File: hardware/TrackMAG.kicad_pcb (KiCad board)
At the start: 4 copper layers, 36 x 36 mm, 54 parts, among them J1 USB_C_Socket_USB2.0, J2 Conn_Debug, SW1 SW_RESET, SW2 SW_BOOT, U1 LSM6DS3TR-C, U2 USBLC6-2P6, U3 STM32F103C8T6, U4 LIS2MDL, U5 AMS1117-3.3, Y1 16MHz

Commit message: Cleanup
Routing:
- net GND: vias 41 -> 44
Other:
- board text added: "TrackMAG v1"
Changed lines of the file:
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@@
     (property "Sheetfile" "TrackMAG.kicad_sch")
     (property "Sheetname" "")
+    (property "exclude_from_bom" "")
     (property "ki_description" "Mounting Hole without connection")
     (property "ki_keywords" "mounting hole")
-    (attr exclude_from_pos_files)
+    (attr exclude_from_pos_files exclude_from_bom)
     (fp_text reference "H2" (at 0 -3.2) (layer "F.SilkS") hide
         (effects (font (size 1 1) (thickness 0.15)))
@@
     (fp_line (start 1 0.625) (end -1 0.625)
       (stroke (width 0.1) (type solid)) (layer "F.Fab"))
-    (pad "1" smd roundrect (at -0.9125 0 90) (size 1.025 1.4) (layers "F.Cu" "F.Paste" "F.Mask") (roundrect_rratio 0.243902)
+    (pad "1" smd roundrect (at -0.9125 0 90) (size 1.025 1.4) (layers "F.Cu" "F.Paste" "F.Mask") (roundrect_rratio 0.243902439)
       (net 6 "VBUS") (pintype "passive"))
-    (pad "2" smd roundrect (at 0.9125 0 90) (size 1.025 1.4) (layers "F.Cu" "F.Paste" "F.Mask") (roundrect_rratio 0.243902)
+    (pad "2" smd roundrect (at 0.9125 0 90) (size 1.025 1.4) (layers "F.Cu" "F.Paste" "F.Mask") (roundrect_rratio 0.243902439)
       (net 57 "+5V") (pintype "passive"))
     (model "${KICAD6_3DMODEL_DIR}/Resistor_SMD.3dshapes/R_0805_2012Metric.wrl"
@@
     (fp_line (start 1.6 0.8) (end 1.6 -0.8)
       (stroke (width 0.1) (type solid)) (layer "F.Fab"))
-    (pad "1" smd roundrect (at -1.35 0) (size 1.4 1.35) (layers "F.Cu" "F.Paste" "F.Mask") (roundrect_rratio 0.185185)
+    (pad "1" smd roundrect (at -1.35 0) (size 1.4 1.35) (layers "F.Cu" "F.Paste" "F.Mask") (roundrect_rratio 0.1851851852)
       (net 6 "VBUS") (pintype "passive"))
-    (pad "2" smd roundrect (at 1.35 0) (size 1.4 1.35) (layers "F.Cu" "F.Paste" "F.Mask") (roundrect_rratio 0.185185)
+    (pad "2" smd roundrect (at 1.35 0) (size 1.4 1.35) (layers "F.Cu" "F.Paste" "F.Mask") (roundrect_rratio 0.1851851852)
       (net 2 "GND") (pintype "passive"))
     (model "${KICAD6_3DMODEL_DIR}/Capacitor_Tantalum_SMD.3dshapes/CP_EIA-3216-18_Kemet-A.wrl"
@@
     (descr "LED SMD 0603 (1608 Metric), square (rectangular) end terminal, IPC_7351 nominal, (Body size source: http://www.tortai-tech.com/upload/download/2011102023233369053.pdf), generated with kicad-footprint-generator")
     (tags "LED")
+    (property "JLCPCB Part #" "C2286")
     (property "Sheetfile" "TrackMAG.kicad_sch")
     (property "Sheetname" "")
@@
     (property "Sheetfile" "TrackMAG.kicad_sch")
     (property "Sheetname" "")
+    (property "exclude_from_bom" "")
     (property "ki_description" "Mounting Hole without connection")
     (property "ki_keywords" "mounting hole")
-    (attr exclude_from_pos_files)
+    (attr exclude_from_pos_files exclude_from_bom)
     (fp_text reference "H1" (at 0 -3.2) (layer "F.SilkS") hide
         (effects (font (size 1 1) (thickness 0.15)))
@@
     (fp_line (start 1.6 0.8) (end 1.6 -0.8)
       (stroke (width 0.1) (type solid)) (layer "F.Fab"))
-    (pad "1" smd roundrect (at -1.35 0) (size 1.4 1.35) (layers "F.Cu" "F.Paste" "F.Mask") (roundrect_rratio 0.185185)
+    (pad "1" smd roundrect (at -1.35 0) (size 1.4 1.35) (layers "F.Cu" "F.Paste" "F.Mask") (roundrect_rratio 0.1851851852)
       (net 1 "+3.3V") (pintype "passive"))
-    (pad "2" smd roundrect (at 1.35 0) (size 1.4 1.35) (layers "F.Cu" "F.Paste" "F.Mask") (roundrect_rratio 0.185185)
+    (pad "2" smd roundrect (at 1.35 0) (size 1.4 1.35) (layers "F.Cu" "F.Paste" "F.Mask") (roundrect_rratio 0.1851851852)
       (net 2 "GND") (pintype "passive"))
     (model "${KICAD6_3DMODEL_DIR}/Capacitor_Tantalum_SMD.3dshapes/CP_EIA-3216-18_Kemet-A.wrl"
@@
     (property "Sheetfile" "TrackMAG.kicad_sch")
     (property "Sheetname" "")
+    (property "exclude_from_bom" "")
     (property "ki_description" "Mounting Hole without connection")
     (property "ki_keywords" "mounting hole")
-    (attr exclude_from_pos_files)
+    (attr exclude_from_pos_files exclude_from_bom)
     (fp_text reference "H3" (at 0 -3.2) (layer "F.SilkS") hide
         (effects (font (size 1 1) (thickness 0.15)))
@@
   (gr_line (start 40.8 68) (end 70.8 68)
     (stroke (width 0.1) (type default)) (layer "Edge.Cuts"))
+  (gr_text "TrackMAG v1" (at 38.25 37.25 -90) (layer "F.SilkS" knockout)
+    (effects (font (size 1 1) (thickness 0.2) bold) (justify left bottom))
+  )
   (segment (start 51.4 39.95) (end 51.4 33.975) (width 0.3) (layer "F.Cu") (net 1))
   (segment (start 45.8 42.575) (end 45.8 42.7) (width 0.3) (layer "F.Cu") (net 1))
@@
   (segment (start 52.15 33.225) (end 46.875 33.225) (width 0.3) (layer "F.Cu") (net 1))
   (segment (start 44.75 44.8045) (end 44.75 46.075) (width 0.3) (layer "F.Cu") (net 1))
-  (segment (start 43.86 34.302943) (end 44.937943 33.225) (width 0.3) (layer "F.Cu") (net 1))
   (segment (start 65.9875 59.0625) (end 66.3875 59.4625) (width 0.2) (layer "F.Cu") (net 1))
   (segment (start 56.8875 54.6875) (end 56.8875 53.717165) (width 0.3) (layer "F.Cu") (net 1))
@@
   (segment (start 49.6 45) (end 49.6 44.7) (width 0.3) (layer "F.Cu") (net 1))
   (segment (start 52.775 41.425) (end 52.825 41.375) (width 0.3) (layer "F.Cu") (net 1))
+  (segment (start 43.8305 34.332443) (end 44.937943 33.225) (width 0.3) (layer "F.Cu") (net 1))
   (segment (start 53.3875 56.3105) (end 53.477 56.4) (width 0.3) (layer "F.Cu") (net 1))
   (segment (start 62.45 56.635) (end 66.385 56.635) (width 0.3) (layer "F.Cu") (net 1))
@@
   (segment (start 67.0625 58.3375) (end 66.1425 58.3375) (width 0.3) (layer "F.Cu") (net 1))
   (segment (start 67.3875 60.9875) (end 67.3875 61.5375) (width 0.25) (layer "F.Cu") (net 1))
-  (segment (start 43.86 40.635) (end 43.86 34.302943) (width 0.3) (layer "F.Cu") (net 1))
   (segment (start 45 65.125) (end 43.05 63.175) (width 0.3) (layer "F.Cu") (net 1))
   (segment (start 52.298 56.4) (end 51.375 57.323) (width 0.3) (layer "F.Cu") (net 1))
@@
   (segment (start 59.875 47.775) (end 60.075 47.575) (width 0.3) (layer "F.Cu") (net 1))
   (segment (start 49.55 57.99) (end 50.135 58.575) (width 0.3) (layer "F.Cu") (net 1))
+  (segment (start 45.8 42.625) (end 43.8305 40.6555) (width 0.3) (layer "F.Cu") (net 1))
   (segment (start 39.475 54.025) (end 38.725 53.275) (width 0.3) (layer "F.Cu") (net 1))
   (segment (start 46.425 47.75) (end 48.17 47.75) (width 0.3) (layer "F.Cu") (net 1))
@@
   (segment (start 48.17 47.75) (end 48.175 47.755) (width 0.3) (layer "F.Cu") (net 1))
   (segment (start 60.075 44.6) (end 60.075 47.575) (width 0.3) (layer "F.Cu") (net 1))
+  (segment (start 43.8305 40.6555) (end 43.8305 34.332443) (width 0.3) (layer "F.Cu") (net 1))
   (segment (start 67.3875 61.5375) (end 67.125 61.8) (width 0.25) (layer "F.Cu") (net 1))
   (segment (start 67.8875 63.5325) (end 68.2925 63.5325) (width 0.3) (layer "F.Cu") (net 1))
@@
   (segment (start 68.5 63.325) (end 68.5 61.8) (width 0.3) (layer "F.Cu") (net 1))
   (segment (start 45.2 65.125) (end 51.2 65.125) (width 0.3) (layer "F.Cu") (net 1))
-  (segment (start 43.86 40.635) (end 45.8 42.575) (width 0.3) (layer "F.Cu") (net 1))
   (segment (start 66.3875 56.6375) (end 66.3875 58.0925) (width 0.3) (layer "F.Cu") (net 1))
   (segment (start 63.88 60.725) (end 65.125 60.725) (width 0.25) (layer "F.Cu") (net 1))
@@
   (segment (start 63.2175 57.9025) (end 63.0775 57.7625) (width 0.3) (layer "F.Cu") (net 2))
   (via (at 54.5 56.4) (size 0.8) (drill 0.4) (layers "F.Cu" "B.Cu") (free) (net 2))
+  (via (at 49.55 54.2) (size 0.8) (drill 0.4) (layers "F.Cu" "B.Cu") (free) (net 2))
   (via (at 49.135497 58.575) (size 0.8) (drill 0.4) (layers "F.Cu" "B.Cu") (free) (net 2))
   (via (at 65.4125 61.7875) (size 0.8) (drill 0.4) (layers "F.Cu" "B.Cu") (net 2))
@@
   (via (at 55.638553 53.373315) (size 0.8) (drill 0.4) (layers "F.Cu" "B.Cu") (net 2))
   (via (at 44.75 42.625) (size 0.8) (drill 0.4) (layers "F.Cu" "B.Cu") (free) (net 2))
+  (via (at 58.475 55.8) (size 0.8) (drill 0.4) (layers "F.Cu" "B.Cu") (free) (net 2))
   (via (at 63.575 54.15) (size 0.8) (drill 0.4) (layers "F.Cu" "B.Cu") (net 2))
   (via (at 43.875 45.4) (size 0.8) (drill 0.4) (layers "F.Cu" "B.Cu") (free) (net 2))
@@
   (via (at 57.375 42.5) (size 0.8) (drill 0.4) (layers "F.Cu" "B.Cu") (free) (net 2))
   (via (at 71.525 50.025) (size 0.8) (drill 0.4) (layers "F.Cu" "B.Cu") (net 2))
+  (via (at 44.4705 39.7) (size 0.8) (drill 0.4) (layers "F.Cu" "B.Cu") (free) (net 2))
   (via (at 54.125 51.85) (size 0.8) (drill 0.4) (layers "F.Cu" "B.Cu") (free) (net 2))
   (via (at 43.2 47.7) (size 0.8) (drill 0.4) (layers "F.Cu" "B.Cu") (net 2))

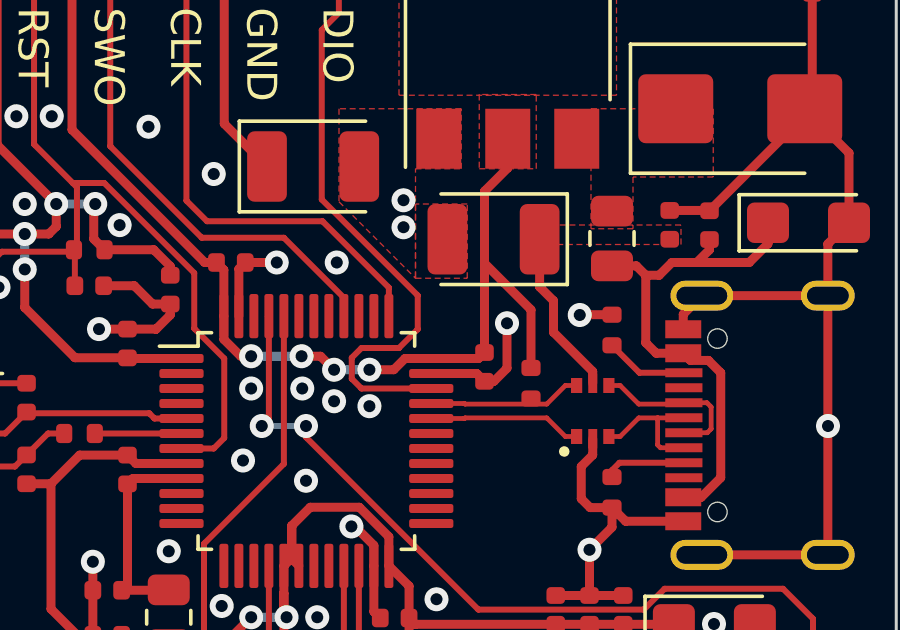
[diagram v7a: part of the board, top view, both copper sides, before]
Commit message: Update schematic PDF and minor PCB cleanup
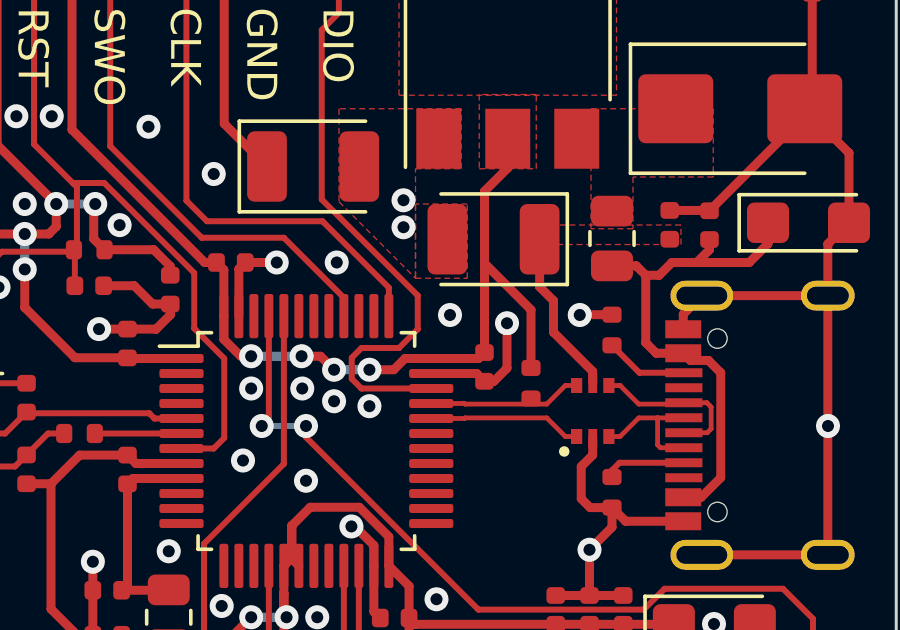
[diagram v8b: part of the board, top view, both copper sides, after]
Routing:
- net GND: vias 44 -> 45
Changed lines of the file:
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@@
   (via (at 54.5 56.4) (size 0.8) (drill 0.4) (layers "F.Cu" "B.Cu") (free) (net 2))
   (via (at 49.55 54.2) (size 0.8) (drill 0.4) (layers "F.Cu" "B.Cu") (free) (net 2))
+  (via (at 58.925 46.325) (size 0.8) (drill 0.4) (layers "F.Cu" "B.Cu") (free) (net 2))
   (via (at 49.135497 58.575) (size 0.8) (drill 0.4) (layers "F.Cu" "B.Cu") (free) (net 2))
   (via (at 65.4125 61.7875) (size 0.8) (drill 0.4) (layers "F.Cu" "B.Cu") (net 2))
